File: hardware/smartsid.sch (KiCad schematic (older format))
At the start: 49 parts, among them P1 INPUT, P2 CONTROL, P3 POT2, P4 SOCKET, P5 OUTPUT, U1 GAL16V8, U2 SID2, U3 7812, U4 7809, U5 SID1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

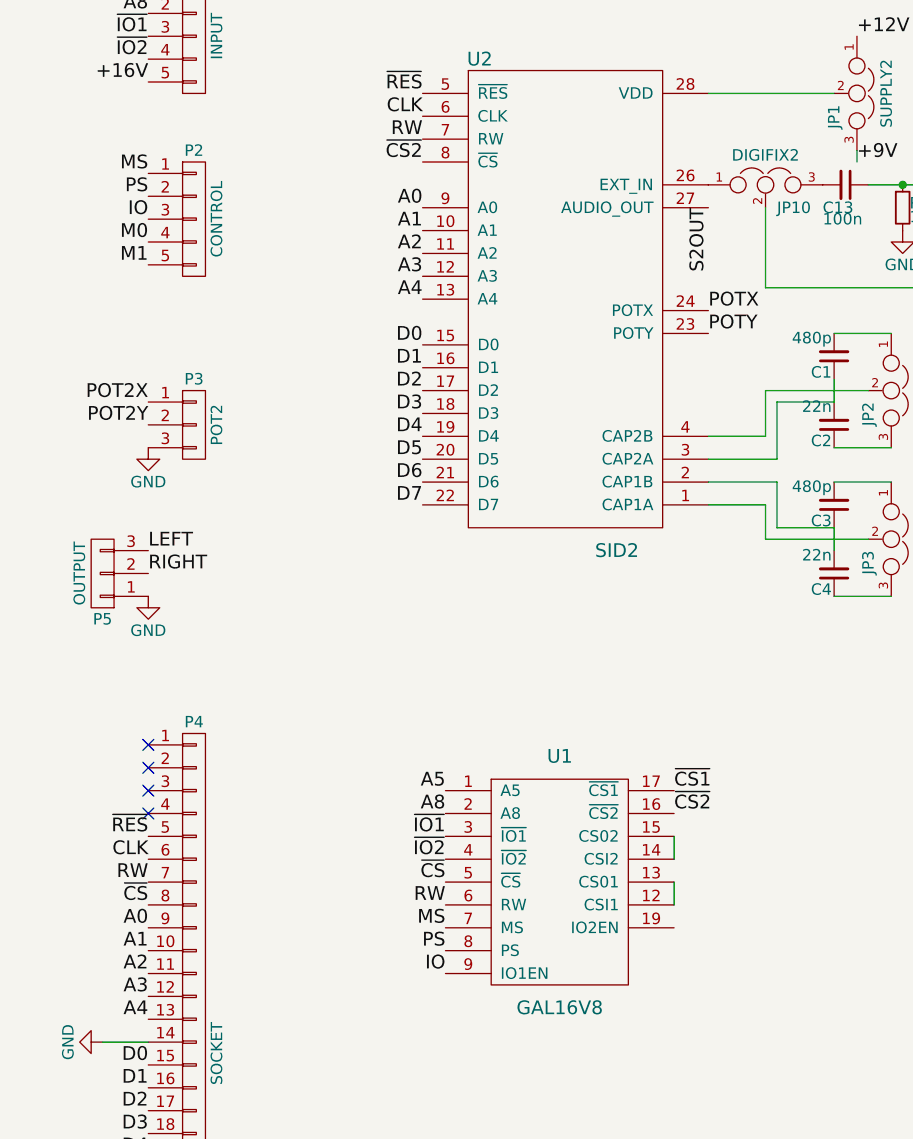
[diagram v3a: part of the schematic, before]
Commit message: Hardware/Firmware: Supply separate IO enable lines (IO1EN, IO2EN)
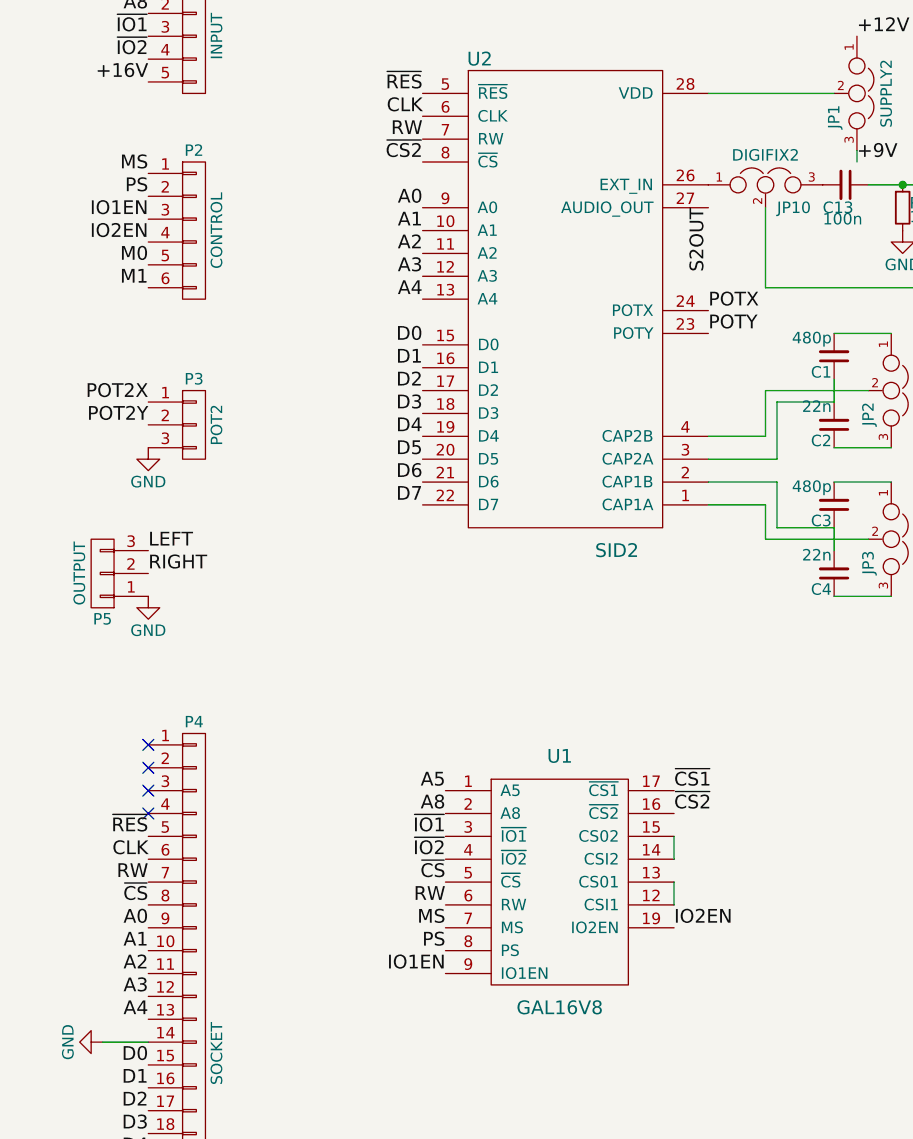
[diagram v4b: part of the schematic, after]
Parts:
- removed P2: CONTROL, Pin_Headers:Pin_Header_Straight_1x05, symbol CONN_01X05
- added P2: CONTROL, Pin_Headers:Pin_Header_Straight_1x06, symbol CONN_01X06
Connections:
- net M0: now also P2.5 (P5)
- net M1: now also P2.6 (P6)
- net MS: now also P2.1 (P1)
- net PS: now also P2.2 (P2)
- net IO2EN: now reaches U1.19 (IO2EN)
- net IO2EN: now also P2.4 (P4)
- net IO renamed IO1EN
- net IO1EN: now also P2.3 (P3)
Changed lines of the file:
@@
 ~IO2
 $Comp
-L PWR_FLAG #FLG1
+L PWR_FLAG #FLG01
 U 1 1 56D823F5
 P 700 7550
-F 0 "#FLG1" H 700 7645 50  0001 C CNN
+F 0 "#FLG01" H 700 7645 50  0001 C CNN
 F 1 "PWR_FLAG" H 700 7730 50  0000 C CNN
 F 2 "" H 700 7550 60  0000 C CNN
@@
 $EndComp
 $Comp
-L VCC #PWR1
+L VCC #PWR02
 U 1 1 56D8247C
 P 700 7550
-F 0 "#PWR1" H 700 7400 50  0001 C CNN
+F 0 "#PWR02" H 700 7400 50  0001 C CNN
 F 1 "VCC" H 700 7700 50  0000 C CNN
 F 2 "" H 700 7550 60  0000 C CNN
@@
 $EndComp
 $Comp
-L PWR_FLAG #FLG2
+L PWR_FLAG #FLG03
 U 1 1 56D8249D
 P 900 7550
-F 0 "#FLG2" H 900 7645 50  0001 C CNN
+F 0 "#FLG03" H 900 7645 50  0001 C CNN
 F 1 "PWR_FLAG" H 900 7730 50  0000 C CNN
 F 2 "" H 900 7550 60  0000 C CNN
@@
 $EndComp
 $Comp
-L GND #PWR4
+L GND #PWR04
 U 1 1 56D824B4
 P 900 7550
-F 0 "#PWR4" H 900 7300 50  0001 C CNN
+F 0 "#PWR04" H 900 7300 50  0001 C CNN
 F 1 "GND" H 900 7400 50  0000 C CNN
 F 2 "" H 900 7550 60  0000 C CNN
@@
 PS
 Text Label 2350 5200 2    60   ~ 0
-IO
+IO1EN
 Text Label 1050 1700 2    60   ~ 0
 MS
@@
 PS
 Text Label 1050 1900 2    60   ~ 0
-IO
+IO1EN
 $Comp
 L CONN_01X03 P3
@@
 $EndComp
 $Comp
-L GND #PWR5
+L GND #PWR05
 U 1 1 56D8560C
 P 1050 2900
-F 0 "#PWR5" H 1050 2650 50  0001 C CNN
+F 0 "#PWR05" H 1050 2650 50  0001 C CNN
 F 1 "GND" H 1050 2750 50  0000 C CNN
 F 2 "" H 1050 2900 60  0000 C CNN
@@
 $EndComp
 $Comp
-L GND #PWR9
+L GND #PWR06
 U 1 1 56D8E33C
 P 3400 7250
-F 0 "#PWR9" H 3400 7000 50  0001 C CNN
+F 0 "#PWR06" H 3400 7000 50  0001 C CNN
 F 1 "GND" H 3400 7100 50  0000 C CNN
 F 2 "" H 3400 7250 60  0000 C CNN
@@
 $EndComp
 $Comp
-L GND #PWR14
+L GND #PWR07
 U 1 1 56D8F791
 P 5150 7250
-F 0 "#PWR14" H 5150 7000 50  0001 C CNN
+F 0 "#PWR07" H 5150 7000 50  0001 C CNN
 F 1 "GND" H 5150 7100 50  0000 C CNN
 F 2 "" H 5150 7250 60  0000 C CNN
@@
 POTX
 $Comp
-L VCC #PWR2
+L VCC #PWR08
 U 1 1 56D974B1
 P 800 6600
-F 0 "#PWR2" H 800 6450 50  0001 C CNN
+F 0 "#PWR08" H 800 6450 50  0001 C CNN
 F 1 "VCC" H 800 6750 50  0000 C CNN
 F 2 "" H 800 6600 60  0000 C CNN
@@
 $EndComp
 $Comp
-L GND #PWR3
+L GND #PWR09
 U 1 1 56D9751E
 P 850 5500
-F 0 "#PWR3" H 850 5250 50  0001 C CNN
+F 0 "#PWR09" H 850 5250 50  0001 C CNN
 F 1 "GND" H 850 5350 50  0000 C CNN
 F 2 "" H 850 5500 60  0000 C CNN
@@
 NoConn ~ 1050 6800
 $Comp
-L VDD #PWR7
+L VDD #PWR010
 U 1 1 56D9CAE7
 P 1050 6900
-F 0 "#PWR7" H 1050 6750 50  0001 C CNN
+F 0 "#PWR010" H 1050 6750 50  0001 C CNN
 F 1 "VDD" H 1050 7050 50  0000 C CNN
 F 2 "" H 1050 6900 60  0000 C CNN
@@
 $EndComp
 $Comp
-L PWR_FLAG #FLG3
+L PWR_FLAG #FLG011
 U 1 1 56D9EC00
 P 1100 7550
-F 0 "#FLG3" H 1100 7645 50  0001 C CNN
+F 0 "#FLG011" H 1100 7645 50  0001 C CNN
 F 1 "PWR_FLAG" H 1100 7730 50  0000 C CNN
 F 2 "" H 1100 7550 60  0000 C CNN
@@
 $EndComp
 $Comp
-L VDD #PWR8
+L VDD #PWR012
 U 1 1 56D9EC5F
 P 1100 7550
-F 0 "#PWR8" H 1100 7400 50  0001 C CNN
+F 0 "#PWR012" H 1100 7400 50  0001 C CNN
 F 1 "VDD" H 1100 7700 50  0000 C CNN
 F 2 "" H 1100 7550 60  0000 C CNN
@@
 $EndComp
 $Comp
-L VDD #PWR11
+L VDD #PWR013
 U 1 1 56D9EE0E
 P 4400 6950
-F 0 "#PWR11" H 4400 6800 50  0001 C CNN
+F 0 "#PWR013" H 4400 6800 50  0001 C CNN
 F 1 "VDD" H 4400 7100 50  0000 C CNN
 F 2 "" H 4400 6950 60  0000 C CNN
@@
 $EndComp
 $Comp
-L GND #PWR18
+L GND #PWR014
 U 1 1 56DA47B4
 P 8550 1900
-F 0 "#PWR18" H 8550 1650 50  0001 C CNN
+F 0 "#PWR014" H 8550 1650 50  0001 C CNN
 F 1 "GND" H 8550 1750 50  0000 C CNN
 F 2 "" H 8550 1900 60  0000 C CNN
@@
 $EndComp
 $Comp
-L GND #PWR22
+L GND #PWR015
 U 1 1 56DA4C29
 P 9400 1900
-F 0 "#PWR22" H 9400 1650 50  0001 C CNN
+F 0 "#PWR015" H 9400 1650 50  0001 C CNN
 F 1 "GND" H 9400 1750 50  0000 C CNN
 F 2 "" H 9400 1900 60  0000 C CNN
@@
 $EndComp
 $Comp
-L GND #PWR10
+L GND #PWR016
 U 1 1 56DA5AEE
 P 4350 1950
-F 0 "#PWR10" H 4350 1700 50  0001 C CNN
+F 0 "#PWR016" H 4350 1700 50  0001 C CNN
 F 1 "GND" H 4350 1800 50  0000 C CNN
 F 2 "" H 4350 1950 60  0000 C CNN
@@
 $EndComp
 $Comp
-L GND #PWR15
+L GND #PWR017
 U 1 1 56DA5AFB
 P 5200 1950
-F 0 "#PWR15" H 5200 1700 50  0001 C CNN
+F 0 "#PWR017" H 5200 1700 50  0001 C CNN
 F 1 "GND" H 5200 1800 50  0000 C CNN
 F 2 "" H 5200 1950 60  0000 C CNN
@@
 $EndComp
 $Comp
-L GND #PWR6
+L GND #PWR018
 U 1 1 56DA641A
 P 1050 3550
-F 0 "#PWR6" H 1050 3300 50  0001 C CNN
+F 0 "#PWR018" H 1050 3300 50  0001 C CNN
 F 1 "GND" H 1050 3400 50  0000 C CNN
 F 2 "" H 1050 3550 60  0000 C CNN
@@
 +12V
 $Comp
-L GND #PWR19
+L GND #PWR019
 U 1 1 56D98271
 P 9000 6000
-F 0 "#PWR19" H 9000 5750 50  0001 C CNN
+F 0 "#PWR019" H 9000 5750 50  0001 C CNN
 F 1 "GND" H 9000 5850 50  0000 C CNN
 F 2 "" H 9000 6000 60  0000 C CNN
@@
 $EndComp
 $Comp
-L GND #PWR23
+L GND #PWR020
 U 1 1 56D98749
 P 9800 5900
-F 0 "#PWR23" H 9800 5650 50  0001 C CNN
+F 0 "#PWR020" H 9800 5650 50  0001 C CNN
 F 1 "GND" H 9800 5750 50  0000 C CNN
 F 2 "" H 9800 5900 60  0000 C CNN
@@
 +12V
 $Comp
-L GND #PWR20
+L GND #PWR021
 U 1 1 56D994FE
 P 9050 4700
-F 0 "#PWR20" H 9050 4450 50  0001 C CNN
+F 0 "#PWR021" H 9050 4450 50  0001 C CNN
 F 1 "GND" H 9050 4550 50  0000 C CNN
 F 2 "" H 9050 4700 60  0000 C CNN
@@
 $EndComp
 $Comp
-L GND #PWR24
+L GND #PWR022
 U 1 1 56D99510
 P 9850 4600
-F 0 "#PWR24" H 9850 4350 50  0001 C CNN
+F 0 "#PWR022" H 9850 4350 50  0001 C CNN
 F 1 "GND" H 9850 4450 50  0000 C CNN
 F 2 "" H 9850 4600 60  0000 C CNN
@@
 $EndComp
 $Comp
-L GND #PWR12
+L GND #PWR023
 U 1 1 56D9AFBD
 P 4700 5250
-F 0 "#PWR12" H 4700 5000 50  0001 C CNN
+F 0 "#PWR023" H 4700 5000 50  0001 C CNN
 F 1 "GND" H 4700 5100 50  0000 C CNN
 F 2 "" H 4700 5250 60  0000 C CNN
@@
 +12V
 $Comp
-L GND #PWR16
+L GND #PWR024
 U 1 1 56D9C967
 P 5400 5600
-F 0 "#PWR16" H 5400 5350 50  0001 C CNN
+F 0 "#PWR024" H 5400 5350 50  0001 C CNN
 F 1 "GND" H 5400 5450 50  0000 C CNN
 F 2 "" H 5400 5600 60  0000 C CNN
@@
 S1OUT
 $Comp
-L GND #PWR17
+L GND #PWR025
 U 1 1 56D9E94B
 P 6100 5450
-F 0 "#PWR17" H 6100 5200 50  0001 C CNN
+F 0 "#PWR025" H 6100 5200 50  0001 C CNN
 F 1 "GND" H 6100 5300 50  0000 C CNN
 F 2 "" H 6100 5450 60  0000 C CNN
@@
 	1    0    0    -1
 $EndComp
-$Comp
-L CONN_01X05 P2
-U 1 1 56D9EFCC
-P 1250 1900
-F 0 "P2" H 1250 2200 50  0000 C CNN
-F 1 "CONTROL" V 1350 1900 50  0000 C CNN
-F 2 "Pin_Headers:Pin_Header_Straight_1x05" H 1250 1900 60  0001 C CNN
-F 3 "" H 1250 1900 60  0000 C CNN
-	1    1250 1900
-	1    0    0    -1
-$EndComp
-Text Label 1050 2000 2    60   ~ 0
+Text Label 1050 2100 2    60   ~ 0
 M0
-Text Label 1050 2100 2    60   ~ 0
+Text Label 1050 2200 2    60   ~ 0
 M1
 Text Notes 3700 7600 2    60   ~ 0
@@
 $EndComp
 $Comp
-L GND #PWR13
+L GND #PWR026
 U 1 1 56DD67B2
 P 4900 2650
-F 0 "#PWR13" H 4900 2400 50  0001 C CNN
+F 0 "#PWR026" H 4900 2400 50  0001 C CNN
 F 1 "GND" H 4900 2500 50  0000 C CNN
 F 2 "" H 4900 2650 60  0000 C CNN
@@
 $EndComp
 $Comp
-L GND #PWR21
+L GND #PWR027
 U 1 1 56DD4FC3
 P 9100 2600
-F 0 "#PWR21" H 9100 2350 50  0001 C CNN
+F 0 "#PWR027" H 9100 2350 50  0001 C CNN
 F 1 "GND" H 9100 2450 50  0000 C CNN
 F 2 "" H 9100 2600 60  0000 C CNN
@@
 $EndComp
 NoConn ~ 9350 2450
+$Comp
+L CONN_01X06 P2
+U 1 1 56DDD7AE
+P 1250 1950
+F 0 "P2" H 1250 2300 50  0000 C CNN
+F 1 "CONTROL" V 1350 1950 50  0000 C CNN
+F 2 "Pin_Headers:Pin_Header_Straight_1x06" H 1250 1950 60  0001 C CNN
+F 3 "" H 1250 1950 60  0000 C CNN
+	1    1250 1950
+	1    0    0    -1
+$EndComp
+Text Label 1050 2000 2    60   ~ 0
+IO2EN
+Text Label 3350 5000 0    60   ~ 0
+IO2EN
 $EndSCHEMATC

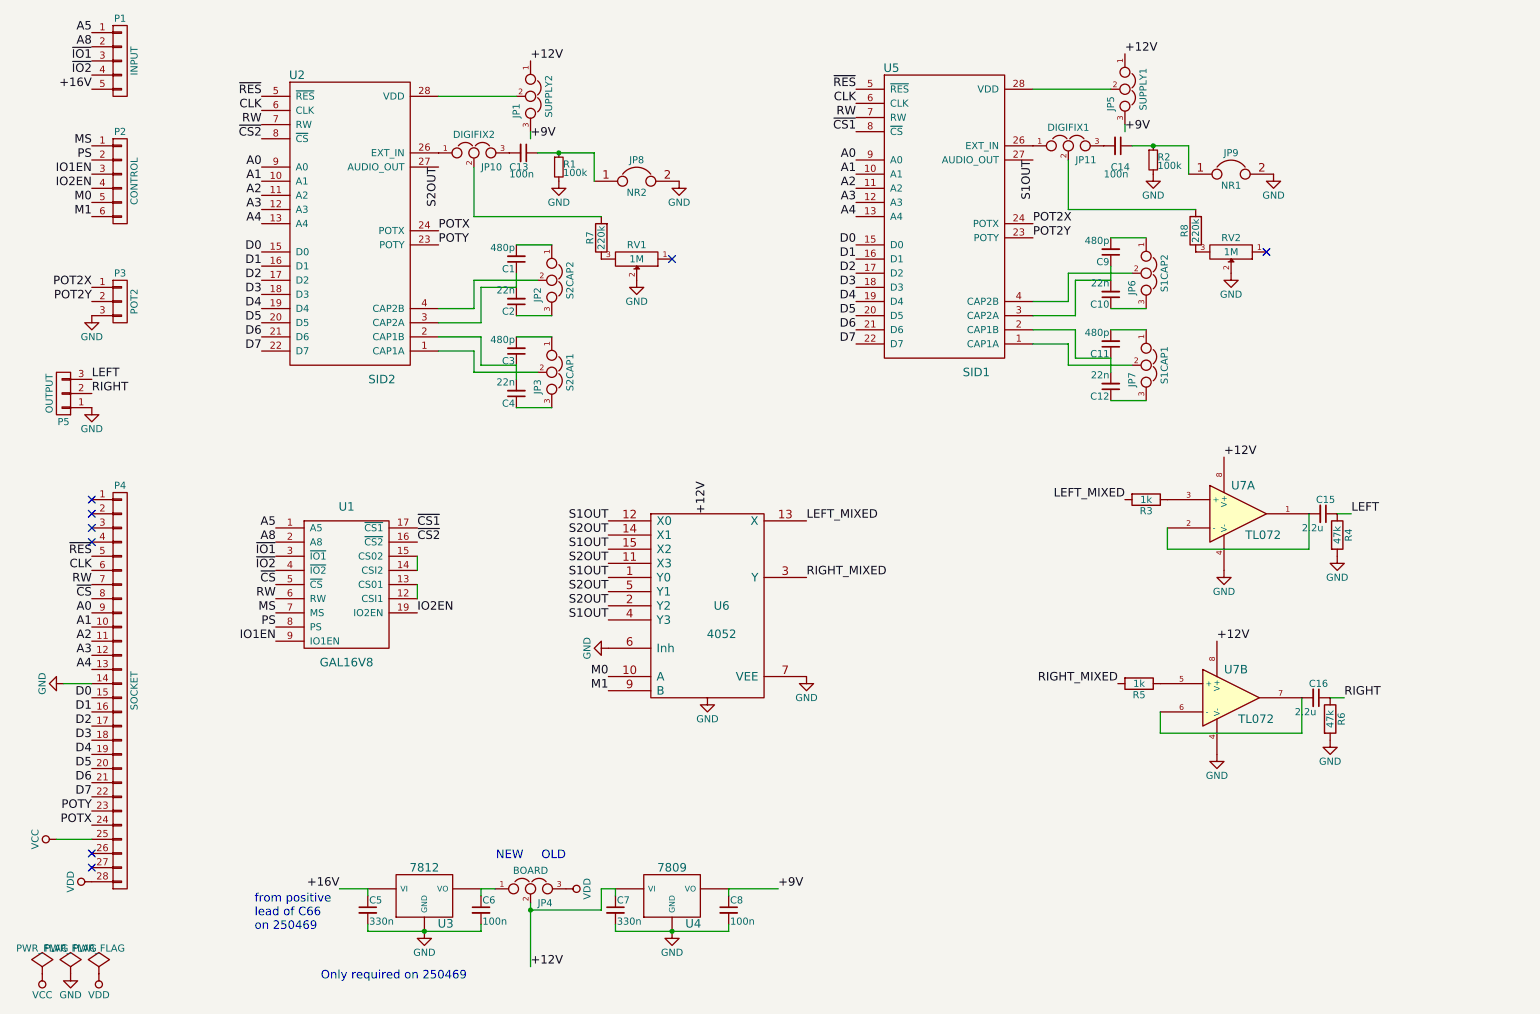
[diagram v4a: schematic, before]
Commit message: Hardware: Removed digifix circuits, added 7660, mix after opamps
The 4052 can only mix signals within 2-8V and VCC must be <10V. Therefore
the amplified output must be mixed.
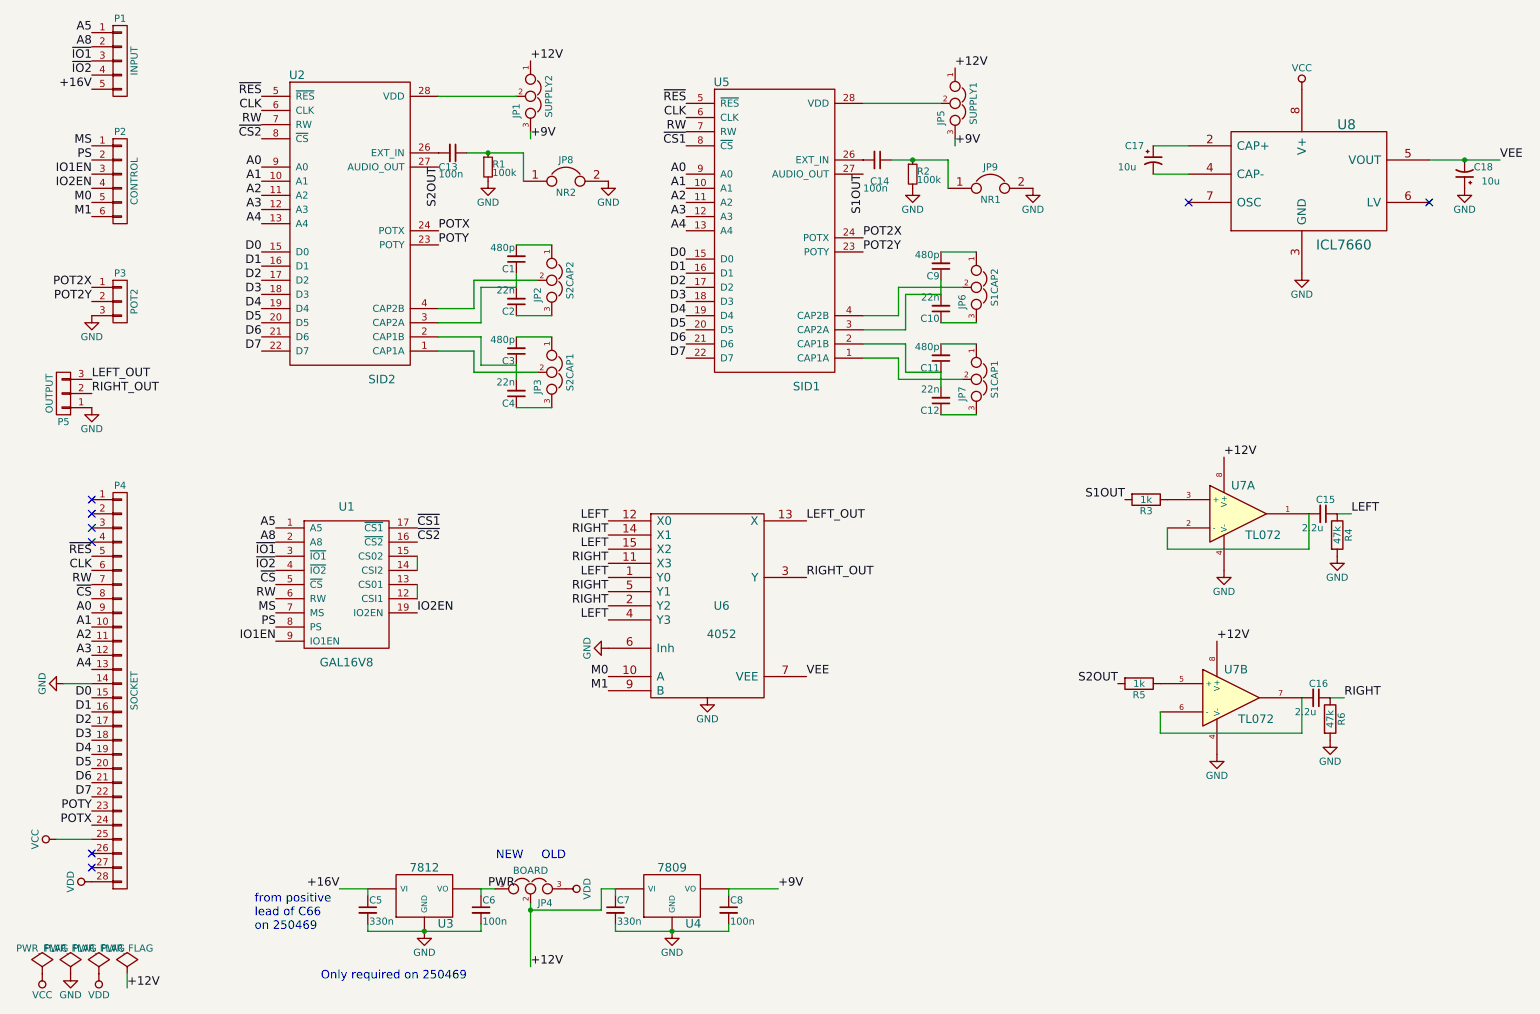
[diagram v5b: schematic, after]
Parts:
- removed JP10: DIGIFIX2, Pin_Headers:Pin_Header_Straight_1x03, symbol JUMPER3
- removed JP11: DIGIFIX1, Pin_Headers:Pin_Header_Straight_1x03, symbol JUMPER3
- removed R7, R8: 220k, Discret:R1, symbol R
- removed RV1, RV2: 1M, Potentiometers:Potentiometer_Bourns_3339H_Angular_ScrewUp, symbol POT
- added C17, C18: 10u, Capacitors_ThroughHole:C_Disc_D3_P2.5, symbol CP1_Small
- added U8: ICL7660, Housings_DIP:DIP-8_W7.62mm, symbol ICL7660
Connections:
- net GND: now also C18.1, U8.3 (GND); no longer U6.7 (VEE)
- net LEFT: now also U6.1 (Y0), U6.12 (X0), U6.15 (X2), U6.4 (Y3); no longer P5.3 (P3)
- net RIGHT: now also U6.11 (X3), U6.14 (X1), U6.2 (Y2), U6.5 (Y1); no longer P5.2 (P2)
- net S1OUT: now also R3.2; no longer U6.1 (Y0), U6.12 (X0), U6.15 (X2), U6.4 (Y3)
- net S2OUT: now also R5.2; no longer U6.11 (X3), U6.14 (X1), U6.2 (Y2), U6.5 (Y1)
- net VCC: now also U8.8 (V+)
- net VDD: no longer C7.1, JP1.1, JP4.2, JP5.1, U4.1 (VI), U7.8 (V+), U7.8 (V+)
- net at U5.26 (EXT_IN): now also C14.2
- net at U2.26 (EXT_IN): now also C13.2
- net PWR: now reaches C6.1, JP4.1, U3.3 (VO)
- net LEFT_MIXED renamed LEFT_OUT
- net LEFT_OUT: now also P5.3 (P3); no longer R3.2
- net RIGHT_MIXED renamed RIGHT_OUT
- net RIGHT_OUT: now also P5.2 (P2); no longer R5.2
- new net: C17.1, U8.2 (CAP+)
- new net: C17.2, U8.4 (CAP-)
- new net +12V: C7.1, JP1.1, JP4.2, JP5.1, U4.1 (VI), U7.8 (V+), U7.8 (V+)
- new net VEE: C18.2, U6.7 (VEE), U8.5 (VOUT)
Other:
- moved on the sheet: C10, C11, C12, C13, C14, C9, JP5, JP6, JP7, JP8, JP9, R1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
